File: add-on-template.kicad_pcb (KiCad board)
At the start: 2 copper layers, 70 x 45 mm, 277 parts, among them J1 Qwiic, J2 Conn_01x04_Male

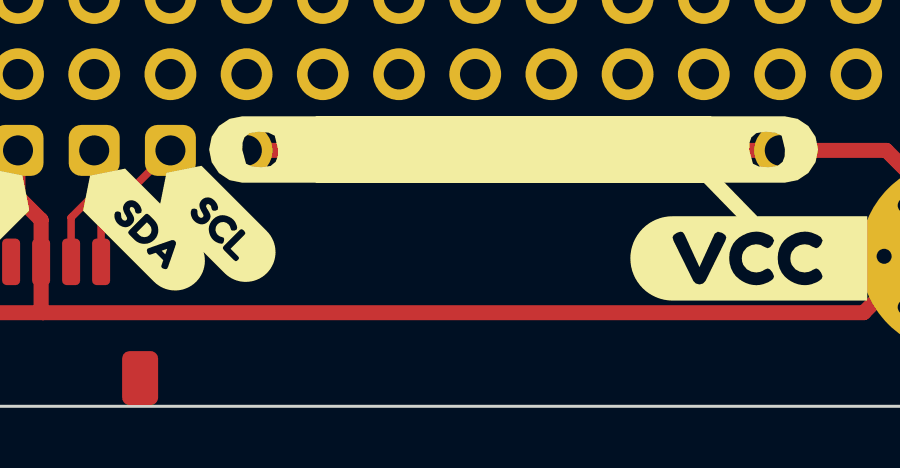
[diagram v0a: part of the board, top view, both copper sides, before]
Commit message: Added readme and gerbers in addition to adding stonsor logo in silkscreen
Signed-off-by: Thomas Flummer <tf@flummer.net>
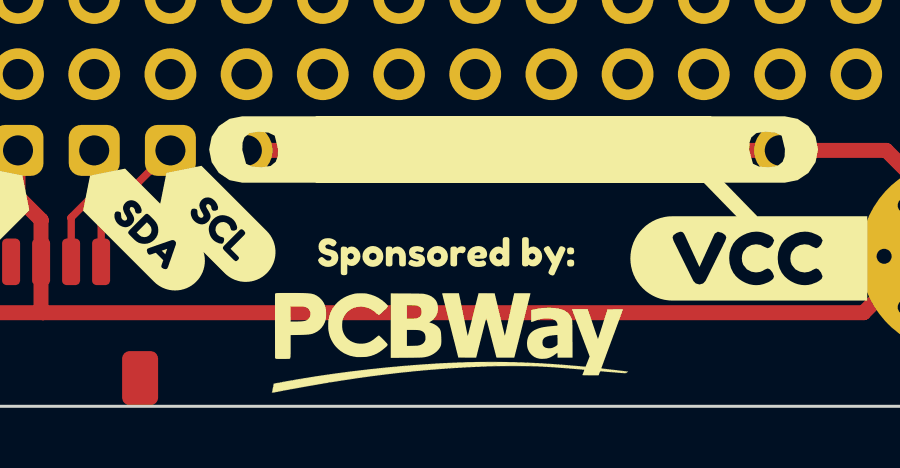
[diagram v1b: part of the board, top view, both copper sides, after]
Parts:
- added G***: LOGO, LOGO, F.Cu at (108.0, 87.8)
- added kibuzzard-62B8370D: G***, kibuzzard-62B8370D, B.Cu at (79.3, 50.0)
- added kibuzzard-62B8371F: G***, kibuzzard-62B8371F, B.Cu at (110.7, 50.0)
- added kibuzzard-62B83731: G***, kibuzzard-62B83731, B.Cu at (118.1, 85.1)
- added kibuzzard-62B83747: G***, kibuzzard-62B83747, B.Cu at (71.8, 85.1)
- added kibuzzard-62C5CE8E: G***, kibuzzard-62C5CE8E, F.Cu at (108.0, 85.0)
